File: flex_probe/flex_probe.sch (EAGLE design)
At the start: 7 parts

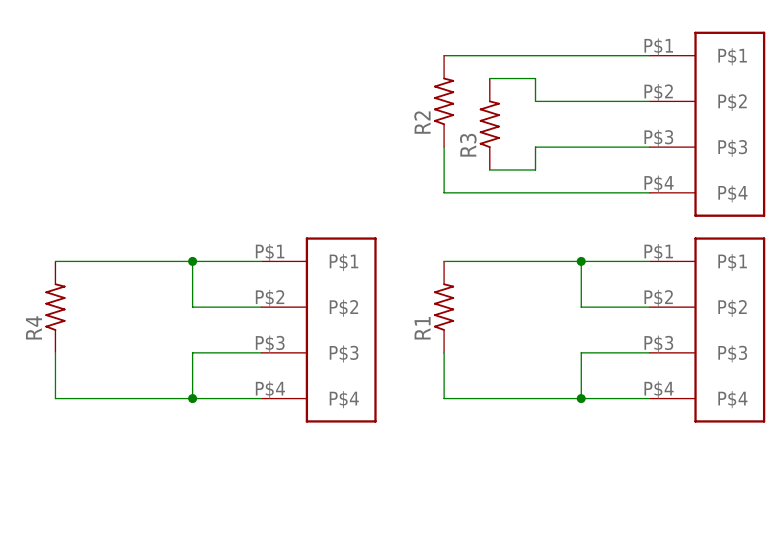
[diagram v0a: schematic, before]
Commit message: New flex PCB.
Shorter length to decrease cost.
Larger trace widths to reduce resistance.
Through-hole connections to make wiring easier
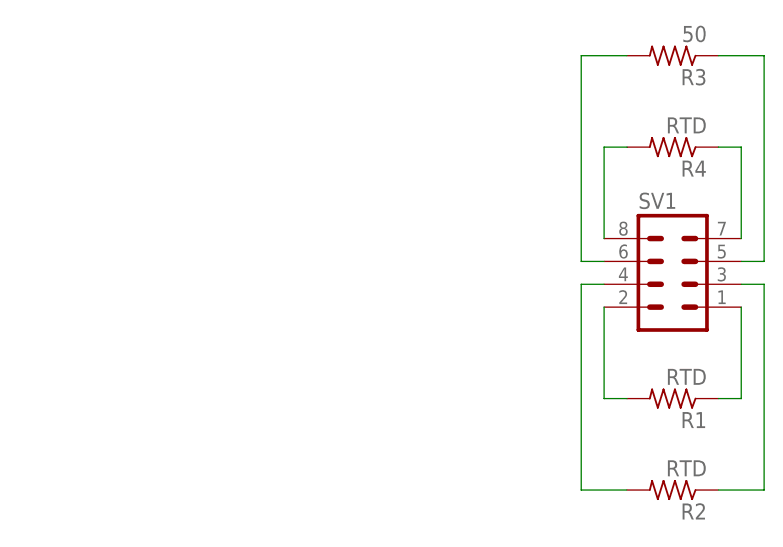
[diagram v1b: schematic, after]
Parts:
- removed U$1, U$2, U$3: CONN_1X4, marshal:CONN_1X4
- added SV1: (no value), con-lstb:MA04-2
- R1, R2, R4: value (none) -> RTD
- R3: value (none) -> 50
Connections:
- removed net N$10: R4.2, U$3.P$1, U$3.P$2
- removed net N$6: R2.1, U$2.P$4
- new net N$3: R2.2, SV1.4
- new net N$4: R2.1, SV1.3
- net N$1: now also SV1.2; no longer U$1.P$1, U$1.P$2
- net N$11: now also R4.2, SV1.8; no longer R4.1, U$3.P$3, U$3.P$4
- net N$2: now also SV1.1; no longer U$1.P$3, U$1.P$4
- net N$7: now also R4.1, SV1.7; no longer R3.2, U$2.P$2
- net N$8: now also R3.2, SV1.6; no longer R3.1, U$2.P$3
- net N$9: now also R3.1, SV1.5; no longer R2.2, U$2.P$1
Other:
- moved on the sheet: R1, R2, R3, R4
